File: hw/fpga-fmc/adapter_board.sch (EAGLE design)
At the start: 175 parts, among them IC1 M24C02, J1 5569262-1, J2 ASP-134488-01, U1 ADM3066E, U10 ADM3066E, U11 ADM3066E, U12 ADM3066E, U13 ADM3066E, U14 ADM3066E, U15 ADM3066E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

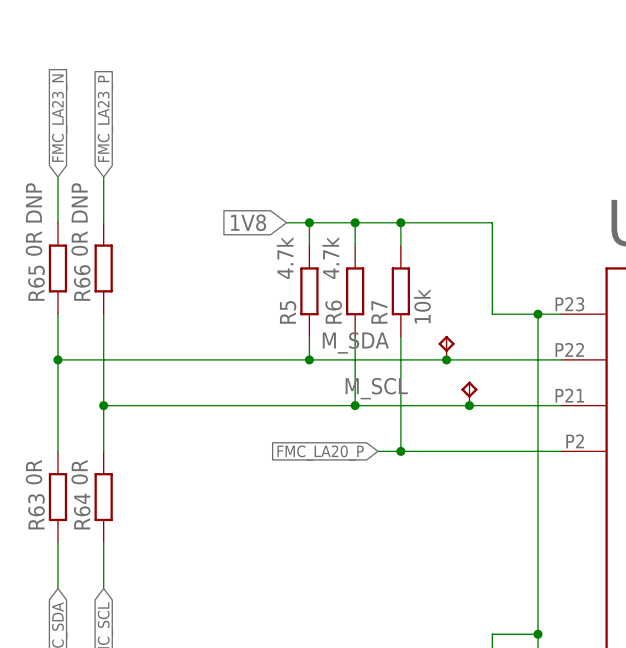
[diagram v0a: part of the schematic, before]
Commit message: hw/fpga-fmc: optimize routing
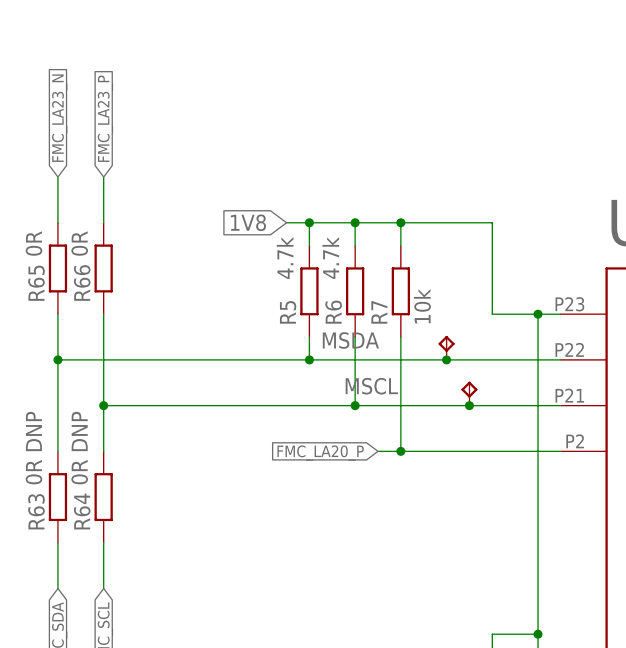
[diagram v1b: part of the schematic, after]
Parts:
- R63, R64: value 0R -> 0R DNP
- R65, R66: value 0R DNP -> 0R
- renumbered M_SCL to MSCL, M_SDA to MSDA
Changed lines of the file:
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@@
 <part name="RJ3_SDO" library="testpad" library_urn="urn:adsk.eagle:library:385" deviceset="TP" device="B1,27" package3d_urn="urn:adsk.eagle:package:27944/2"/>
 <part name="RJ3_SCL" library="testpad" library_urn="urn:adsk.eagle:library:385" deviceset="TP" device="B1,27" package3d_urn="urn:adsk.eagle:package:27944/2"/>
-<part name="M_SDA" library="testpad" library_urn="urn:adsk.eagle:library:385" deviceset="TP" device="B1,27" package3d_urn="urn:adsk.eagle:package:27944/2"/>
-<part name="M_SCL" library="testpad" library_urn="urn:adsk.eagle:library:385" deviceset="TP" device="B1,27" package3d_urn="urn:adsk.eagle:package:27944/2"/>
+<part name="MSDA" library="testpad" library_urn="urn:adsk.eagle:library:385" deviceset="TP" device="B1,27" package3d_urn="urn:adsk.eagle:package:27944/2"/>
+<part name="MSCL" library="testpad" library_urn="urn:adsk.eagle:library:385" deviceset="TP" device="B1,27" package3d_urn="urn:adsk.eagle:package:27944/2"/>
 <part name="RJ1_CONV" library="testpad" library_urn="urn:adsk.eagle:library:385" deviceset="TP" device="B1,27" package3d_urn="urn:adsk.eagle:package:27944/2"/>
 <part name="RJ2_CONV" library="testpad" library_urn="urn:adsk.eagle:library:385" deviceset="TP" device="B1,27" package3d_urn="urn:adsk.eagle:package:27944/2"/>
@@
 <part name="GND77" library="supply1" library_urn="urn:adsk.eagle:library:371" deviceset="0V" device=""/>
 <part name="+3V6" library="supply1" library_urn="urn:adsk.eagle:library:371" deviceset="+3V3" device=""/>
-<part name="R63" library="rcl" library_urn="urn:adsk.eagle:library:334" deviceset="R-EU_" device="R0805" package3d_urn="urn:adsk.eagle:package:23553/2" value="0R"/>
-<part name="R64" library="rcl" library_urn="urn:adsk.eagle:library:334" deviceset="R-EU_" device="R0805" package3d_urn="urn:adsk.eagle:package:23553/2" value="0R"/>
-<part name="R65" library="rcl" library_urn="urn:adsk.eagle:library:334" deviceset="R-EU_" device="R0805" package3d_urn="urn:adsk.eagle:package:23553/2" value="0R DNP"/>
-<part name="R66" library="rcl" library_urn="urn:adsk.eagle:library:334" deviceset="R-EU_" device="R0805" package3d_urn="urn:adsk.eagle:package:23553/2" value="0R DNP"/>
+<part name="R63" library="rcl" library_urn="urn:adsk.eagle:library:334" deviceset="R-EU_" device="R0805" package3d_urn="urn:adsk.eagle:package:23553/2" value="0R DNP"/>
+<part name="R64" library="rcl" library_urn="urn:adsk.eagle:library:334" deviceset="R-EU_" device="R0805" package3d_urn="urn:adsk.eagle:package:23553/2" value="0R DNP"/>
+<part name="R65" library="rcl" library_urn="urn:adsk.eagle:library:334" deviceset="R-EU_" device="R0805" package3d_urn="urn:adsk.eagle:package:23553/2" value="0R"/>
+<part name="R66" library="rcl" library_urn="urn:adsk.eagle:library:334" deviceset="R-EU_" device="R0805" package3d_urn="urn:adsk.eagle:package:23553/2" value="0R"/>
 <part name="JP1" library="pinhead" library_urn="urn:adsk.eagle:library:325" deviceset="PINHD-2X10" device="" package3d_urn="urn:adsk.eagle:package:22405/2"/>
 <part name="GND78" library="supply1" library_urn="urn:adsk.eagle:library:371" deviceset="0V" device=""/>
@@
 <attribute name="TP_SIGNAL_NAME" x="-214.63" y="11.43" size="1.778" layer="97"/>
 </instance>
-<instance part="M_SDA" gate="G$1" x="-297.18" y="22.86" smashed="yes">
+<instance part="MSDA" gate="G$1" x="-297.18" y="22.86" smashed="yes">
 <attribute name="NAME" x="-311.15" y="21.59" size="1.778" layer="95"/>
 <attribute name="TP_SIGNAL_NAME" x="-295.91" y="21.59" size="1.778" layer="97"/>
 </instance>
-<instance part="M_SCL" gate="G$1" x="-294.64" y="17.78" smashed="yes">
+<instance part="MSCL" gate="G$1" x="-294.64" y="17.78" smashed="yes">
 <attribute name="NAME" x="-308.61" y="16.51" size="1.778" layer="95"/>
 <attribute name="TP_SIGNAL_NAME" x="-293.37" y="16.51" size="1.778" layer="97"/>
@@
 <wire x1="-312.42" y1="22.86" x2="-312.42" y2="20.32" width="0.1524" layer="91"/>
 <junction x="-312.42" y="20.32"/>
-<pinref part="M_SDA" gate="G$1" pin="TP"/>
+<pinref part="MSDA" gate="G$1" pin="TP"/>
 <junction x="-297.18" y="20.32"/>
 <pinref part="R65" gate="G$1" pin="1"/>
@@
 <wire x1="-307.34" y1="22.86" x2="-307.34" y2="15.24" width="0.1524" layer="91"/>
 <junction x="-307.34" y="15.24"/>
-<pinref part="M_SCL" gate="G$1" pin="TP"/>
+<pinref part="MSCL" gate="G$1" pin="TP"/>
 <junction x="-294.64" y="15.24"/>
 <pinref part="R66" gate="G$1" pin="1"/>

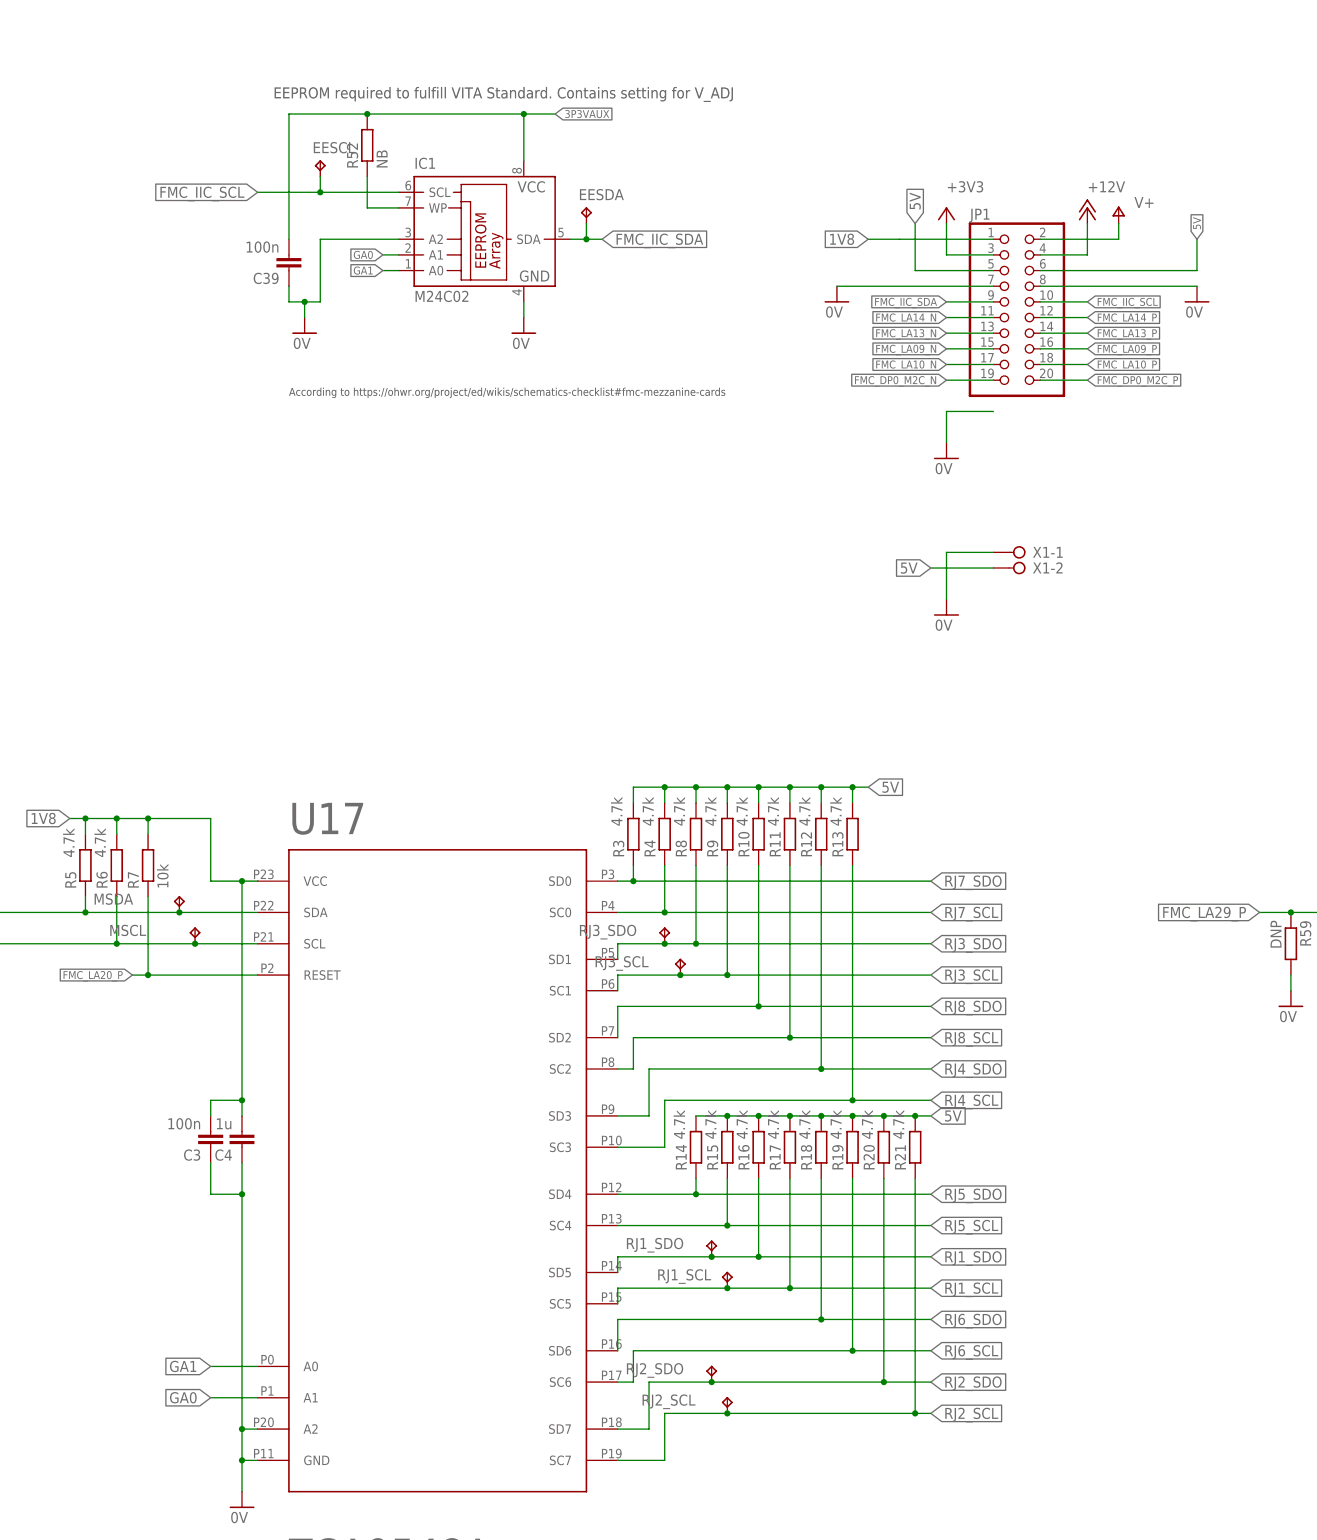
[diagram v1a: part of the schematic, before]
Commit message: hw/fmc minor cleanup in layout and schematic
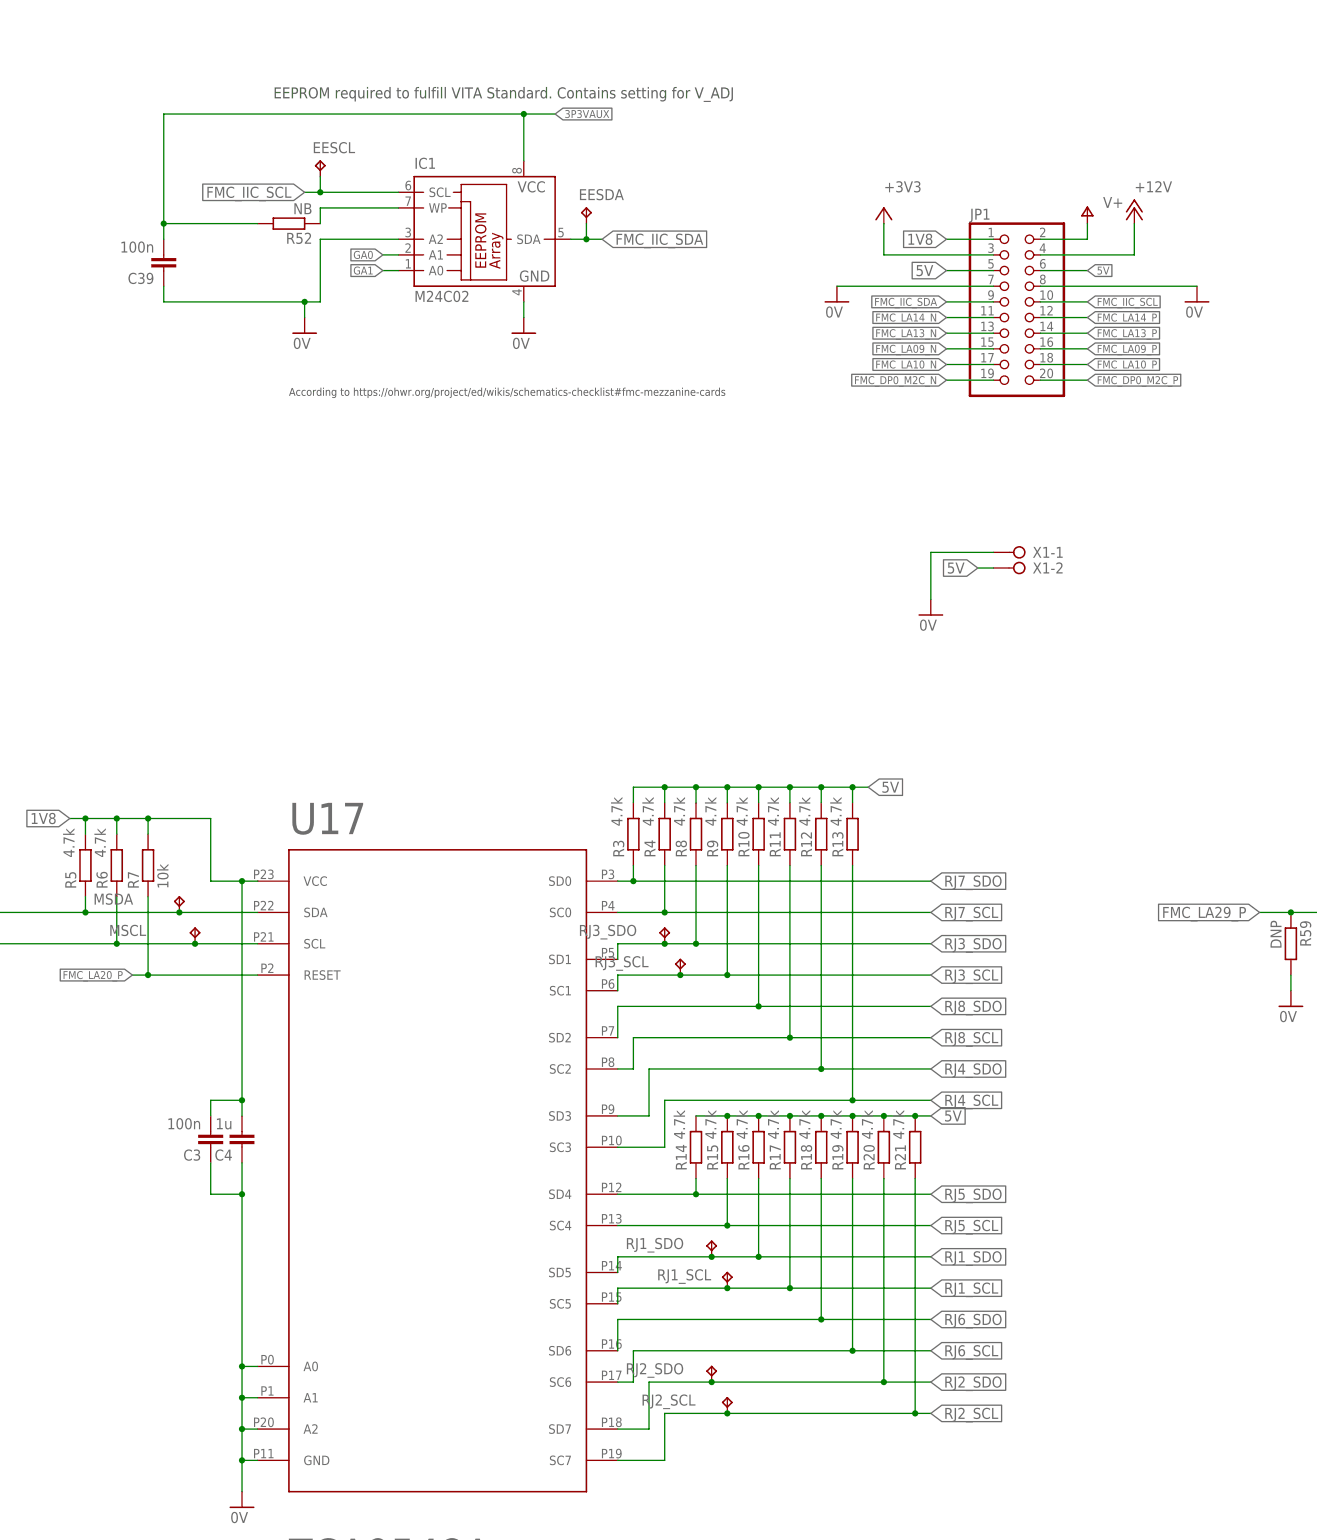
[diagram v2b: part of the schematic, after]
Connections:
- net 0V: now also U17.A0, U17.A1
- net GA0: no longer U17.A1
- net GA1: no longer U17.A0
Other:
- moved on the sheet: C39, R52

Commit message: hw/fpga-fmc: make rs485 termination resistors 0805 for better power rating
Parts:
- R1, R22, R24, R26, R28, R30, R32, R34, R36, R38, R40, R42, R44, R46, R48, R50: device rcl:R-EU_R0603 -> rcl:R-EU_R0805
